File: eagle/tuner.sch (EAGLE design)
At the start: 32 parts, among them IC1 MEGA8-AI, IC2 LM358D, IC3 7805TV, M1 MIC

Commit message: updated PCB
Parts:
- removed M1: MIC, microphon:ELECTRET_MICROPHON-WM.64PN
- removed S1: POWER, switch:TL32YO
- removed S2: (no value), switch-omron:10-XX
- removed SG1: BUZZER, buzzer:F/QMB
- removed TP1, TP2: PTR1B1,27, testpad:PTR1B1,27
- added C10, C14, C15, C22, C23: 0.1uF, eagle-ltspice:C
- added C11, C12, C13: 1uF, eagle-ltspice:C
- added C16, C17, C18, C19: 47uF, rcl:CPOL-EUE2.5-5
- added C20: 470uF, rcl:CPOL-EUE3.5-8
- added C9: 470pF, eagle-ltspice:C
- added IN, OUT: (no value), pinhead:PINHD-1X2
- added R12, R13, R16, R17, R18, R19: 10k, resistor:R-EU_M0805
- added R14, R15: 1k, resistor:R-EU_M0805
- added SEL, VOL: (no value), pinhead:PINHD-1X3
- added U1: LP2985AIM5-5.0, LP2985AIM5-5.0:LP2985AIM5-5.0
- C2: value 0.1uF -> 2.2uF
- IC2: value LM358D -> LM358N; device linear:LM358D -> linear:LM358N
- IC3: value 7805TV -> AD811N; device linear:7805TV -> analog-devices:AD811N
- R10, R4: value 220k -> 10k
- R11: value 220k -> 20k
- R2: value 2.2k -> 100k
- R3: value (none) -> 100k; device resistor:R-TRIMM4G/J -> resistor:R-EU_M0805
- R5, R8: value 2.2k -> 10k
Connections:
- removed net RX: IC1.PD0(RXD), TP1.TP
- removed net TX: IC1.PD1(TXD), TP2.TP
- removed net V/2: IC2A.+IN, IC2B.+IN, R6.2, R7.1
- removed net VCC: C2.1, C3.2, IC1.VCC@1, IC1.VCC@2, IC2P.V+, IC3.VO, L1.1, R1.1, R10.2, R7.2, R8.2, S2.S, S2.S1, SV1.5
- new net 2.5V: C18.-, C19.+, IC2B.+IN, R4.1, R6.2, R7.1
- new net 4.5V: C16.-, C17.+, IC3.IN+, R12.2, R13.1
- new net 5V: C18.+, C2.1, C3.2, C8.2, IC1.VCC@1, IC1.VCC@2, L1.1, R1.1, R18.2, R19.2, R7.2, SV1.5, U1.VOUT
- new net 9V: C1.1, C16.+, G1.+, IC2P.V+, IC3.+VS, R13.2, R3.2, U1.ON/OFF, U1.VIN
- new net CLICK: C10.1, IC1.PD2(INT0)
- new net COUNT: C23.2, IC1.PD7(AIN1), R17.2, R19.1
- new net INSTR: C12.1, IC2A.OUT, R14.2, R4.2, R5.1
- new net N$11: IC3.IN-, R10.2, R11.2, R8.1, R9.2
- new net N$19: C15.1, R15.2, VOL.1
- new net N$20: IC2B.-IN, VOL.2
- new net N$21: C20.-, OUT.2
- new net N$23: R16.1, SEL.1
- new net N$24: R17.1, SEL.3
- new net PHASE: C22.1, IC1.PD6(AIN0), R16.2, R18.1
- new net TUNE: C11.1, IC2B.OUT, VOL.3
- net GND: now also C14.1, C15.2, C17.-, C19.-, C22.2, C23.1, C8.1, C9.2, IC3.-VS, IN.1, OUT.1, R12.1, R2.1, SEL.2, U1.GND; no longer IC3.GND, M1.2, R11.1, R9.1, SG1.-
- net N$10: now also C13.1, IC2A.+IN, R2.2, R3.1; no longer IC1.PC0(ADC0), IC2A.OUT, R3.A
- net N$12: now also C13.2, IN.2; no longer IC2B.OUT, R2.2, R4.1
- net N$13: now also IC2A.-IN, R5.2; no longer IC2B.-IN, R4.2, R5.1
- net N$14: now also C10.2, R9.1; no longer C8.2, M1.1, R8.1
- net N$15: now also C14.2, IC1.PC0(ADC0), R14.1; no longer C8.1, R10.1, R11.2, R5.2
- net N$16: now also C11.2, R10.1; no longer G1.+, S1.P
- net N$17: now also C12.2, R11.1; no longer IC1.PD3(INT1), R9.2, S2.P, S2.P1
- net N$18: now also IC1.PD3(INT1), R15.1; no longer IC2A.-IN, R2.1, R3.S
- net N$2: now also C9.1, U1.BY_PASS; no longer C1.1, IC3.VI, S1.O
- net N$9: now also C20.+, IC3.OUT, R8.2; no longer IC1.PD2(INT0), SG1.+
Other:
- moved on the sheet: C1, C2, C3, C8, G1, IC2A, IC2B, R10, R11, R2, R4, R5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

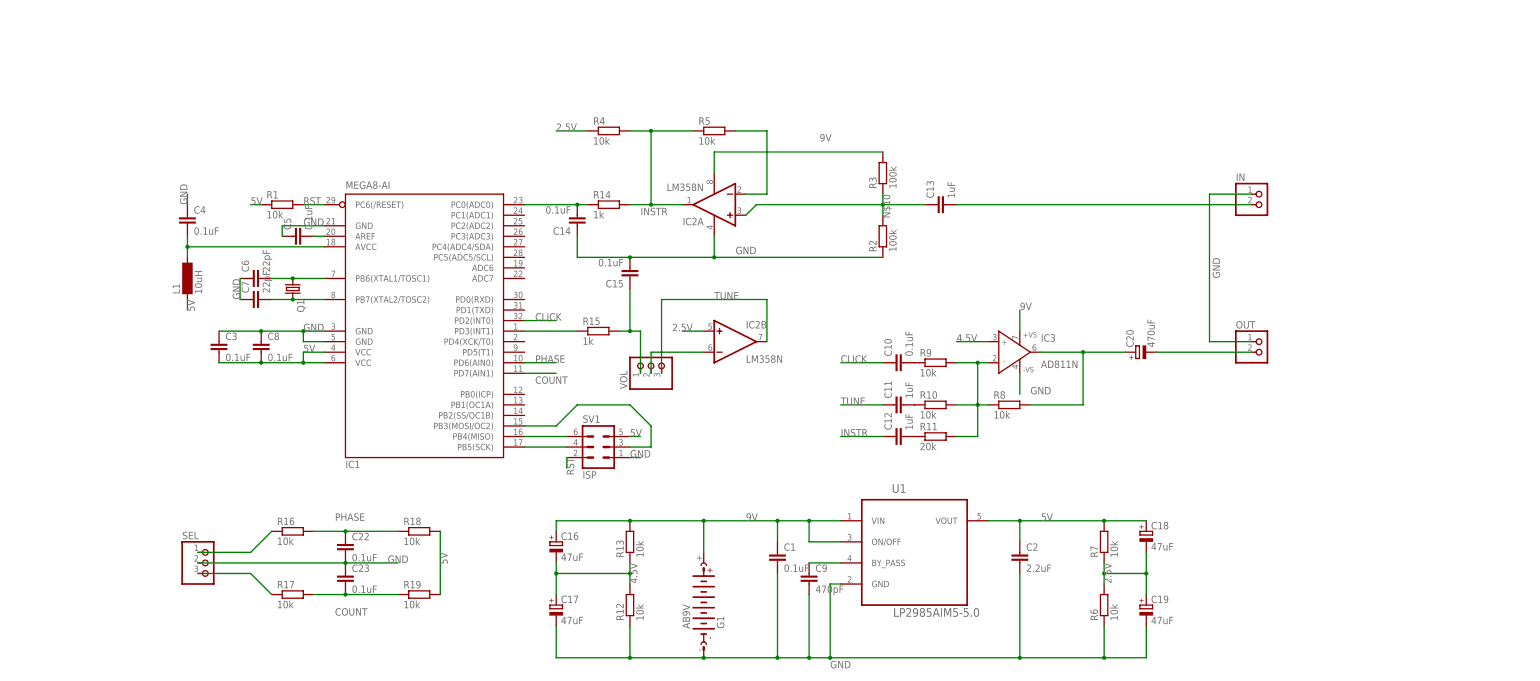
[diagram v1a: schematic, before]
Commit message: update schematic with agc and high-z input, D-class out
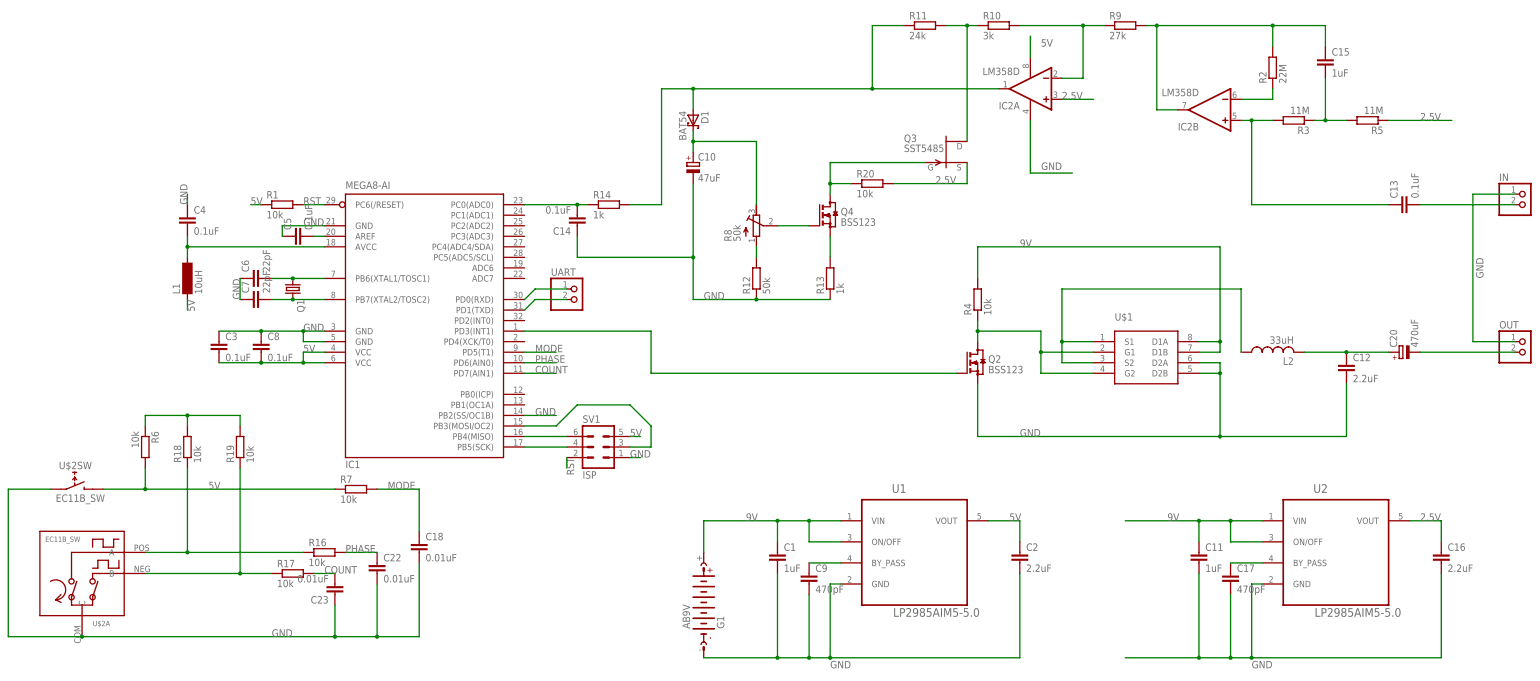
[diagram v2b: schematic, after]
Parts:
- removed C19: 47uF, rcl:CPOL-EUE2.5-5
- removed IC3: AD811N, analog-devices:AD811N
- removed R15: 1k, resistor:R-EU_M0805
- removed SEL, VOL: (no value), pinhead:PINHD-1X3
- added D1: BAT54, diode:BAT54
- added L2: 33uH, rcl:L-US6000-XXX-RC
- added Q2, Q4: BSS123, transistor-small-signal:BSS123
- added Q3: SST5485, transistor-fet:SST5485
- added R20: 10k, resistor:R-EU_M0805
- added U$1: IRF9389TRPBF, IRF9389TRPBF:IRF9389TRPBF
- added U$2: EC11B_SW, rotary-encoder:EC11B_SW
- added U2: LP2985AIM5-5.0, LP2985AIM5-5.0:LP2985AIM5-5.0
- added UART: (no value), pinhead:PINHD-1X2
- C1, C15: value 0.1uF -> 1uF
- C10: value 0.1uF -> 47uF; device eagle-ltspice:C -> rcl:CPOL-EUE2-5
- C12: value 1uF -> 2.2uF
- C13: value 1uF -> 0.1uF
- C16: value 47uF -> 2.2uF; device rcl:CPOL-EUE2.5-5 -> eagle-ltspice:C
- C17: value 47uF -> 470pF; device rcl:CPOL-EUE2.5-5 -> eagle-ltspice:C
- C18: value 47uF -> 0.01uF; device rcl:CPOL-EUE2.5-5 -> eagle-ltspice:C
- C22, C23: value 0.1uF -> 0.01uF
- IC2: value LM358N -> LM358D; device linear:LM358N -> linear:LM358D
- R10: value 10k -> 3k
- R11: value 20k -> 24k
- R12: value 10k -> 50k
- R13: value 10k -> 1k
- R2: value 100k -> 22M
- R3: value 100k -> 11M
- R5: value 10k -> 11M
- R8: value 10k -> 50k; device resistor:R-EU_M0805 -> rcl:R-TRIMM4G/J
- R9: value 10k -> 27k
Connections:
- removed net 4.5V: C16.-, C17.+, IC3.IN+, R12.2, R13.1
- removed net CLICK: C10.1, IC1.PD2(INT0)
- removed net INSTR: C12.1, IC2A.OUT, R14.2, R4.2, R5.1
- removed net TUNE: C11.1, IC2B.OUT, VOL.3
- new net MODE: C18.1, IC1.PD5(T1), R7.2
- new net N$26: IC1.PD0(RXD), UART.1
- new net N$27: D1.A, IC2A.OUT, R11.1, R14.2
- new net N$28: IC1.PD1(TXD), UART.2
- new net N$29: C10.+, D1.C, R8.E
- new net N$30: R12.2, R8.A
- new net N$31: Q4.G, R8.S
- new net N$32: Q4.S, R13.2
- new net N$33: Q3.G, Q4.D, R20.1
- new net N$34: C17.1, U2.BY_PASS
- new net N$35: R6.2, R7.1, U$2SW.E
- net 2.5V: now also C16.1, IC2A.+IN, Q3.S, R20.2, R5.1, U2.VOUT; no longer C18.-, C19.+, IC2B.+IN, R4.1, R6.2, R7.1
- net 5V: now also IC2P.V+, R6.1; no longer C18.+, R7.2
- net 9V: now also C11.1, R4.2, U$1.D1A, U$1.D1B, U2.ON/OFF, U2.VIN; no longer C16.+, IC2P.V+, IC3.+VS, R13.2, R3.2
- net COUNT: no longer R19.1
- net GND: now also C10.-, C11.2, C12.2, C16.2, C17.2, C18.2, IC1.PB2(SS/OC1B), Q2.S, R13.1, U$1.D2A, U$1.D2B, U$2A.C, U$2SW.D, U2.GND; no longer C15.2, C17.-, C19.-, IC3.-VS, R2.1, R6.1, SEL.2
- net N$10: now also C15.1, IC2B.OUT, R9.2; no longer C13.1, IC2A.+IN, R3.1
- net N$11: now also L2.1, U$1.S1, U$1.S2; no longer IC3.IN-, R10.2, R11.2, R8.1, R9.2
- net N$13: now also IC2B.-IN, R2.1; no longer IC2A.-IN, R5.2
- net N$14: now also C12.1, C20.+, L2.2; no longer C10.2, R9.1
- net N$16: now also C13.1, IC2B.+IN, R3.2; no longer C11.2, R10.1
- net N$17: now also C15.2, R3.1, R5.2; no longer C12.2, R11.1
- net N$18: now also Q2.G; no longer R15.1
- net N$19: now also IC2A.-IN, R10.2, R9.1; no longer C15.1, R15.2, VOL.1
- net N$20: now also Q3.D, R10.1, R11.2; no longer IC2B.-IN, VOL.2
- net N$23: now also R18.1, U$2A.A; no longer SEL.1
- net N$24: now also R19.1, U$2A.B; no longer SEL.3
- net N$9: now also Q2.D, R4.1, U$1.G1, U$1.G2; no longer C20.+, IC3.OUT, R8.2
- net PHASE: no longer R18.1
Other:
- moved on the sheet: C11, C12, C13, C15, C20, C22, C23, IC2A, IC2B, IN, OUT, R10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

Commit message: second revision
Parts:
- removed G1: AB9V, battery:AB9V
- added 9V: (no value), pinhead:PINHD-1X2
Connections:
- net 9V: now also 9V.1; no longer G1.+
- net GND: now also 9V.2; no longer G1.-
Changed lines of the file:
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@@
 <parts>
 <part name="IC1" library="atmel" deviceset="MEGA8" device="-AI"/>
-<part name="G1" library="battery" deviceset="AB9V" device=""/>
 <part name="C1" library="eagle-ltspice" deviceset="C" device="" value="1uF"/>
 <part name="C2" library="eagle-ltspice" deviceset="C" device="" value="2.2uF"/>
@@
 <part name="C18" library="eagle-ltspice" deviceset="C" device="" value="0.01uF"/>
 <part name="R7" library="resistor" deviceset="R-EU_" device="M0805" value="10k"/>
+<part name="9V" library="pinhead" library_urn="urn:adsk.eagle:library:325" deviceset="PINHD-1X2" device=""/>
 </parts>
 <sheets>
@@
 <instances>
 <instance part="IC1" gate="G$1" x="27.94" y="58.42"/>
-<instance part="G1" gate="G$1" x="96.52" y="-12.7" rot="MR90"/>
 <instance part="C1" gate="G$1" x="114.3" y="0"/>
 <instance part="C2" gate="G$1" x="172.72" y="0"/>
@@
 <instance part="C18" gate="G$1" x="27.94" y="2.54"/>
 <instance part="R7" gate="G$1" x="12.7" y="15.24"/>
+<instance part="9V" gate="G$1" x="93.98" y="-12.7"/>
 </instances>
 <busses>
@@
 </segment>
 <segment>
-<pinref part="G1" gate="G$1" pin="-"/>
 <wire x1="121.92" y1="-25.4" x2="114.3" y2="-25.4" width="0.1524" layer="91"/>
 <wire x1="114.3" y1="-25.4" x2="96.52" y2="-25.4" width="0.1524" layer="91"/>
@@
 <pinref part="C2" gate="G$1" pin="2"/>
 <wire x1="172.72" y1="-5.08" x2="172.72" y2="-25.4" width="0.1524" layer="91"/>
+<pinref part="9V" gate="G$1" pin="2"/>
+<wire x1="96.52" y1="-25.4" x2="96.52" y2="-12.7" width="0.1524" layer="91"/>
+<wire x1="96.52" y1="-12.7" x2="91.44" y2="-12.7" width="0.1524" layer="91"/>
 </segment>
 <segment>
@@
 <junction x="121.92" y="7.62"/>
 <junction x="114.3" y="7.62"/>
-<pinref part="G1" gate="G$1" pin="+"/>
 <wire x1="96.52" y1="7.62" x2="114.3" y2="7.62" width="0.1524" layer="91"/>
-<wire x1="96.52" y1="0" x2="96.52" y2="7.62" width="0.1524" layer="91"/>
+<pinref part="9V" gate="G$1" pin="1"/>
+<wire x1="96.52" y1="7.62" x2="96.52" y2="-10.16" width="0.1524" layer="91"/>
+<wire x1="96.52" y1="-10.16" x2="91.44" y2="-10.16" width="0.1524" layer="91"/>
 </segment>
 <segment>
@@
 <wire x1="83.82" y1="43.18" x2="83.82" y2="53.34" width="0.1524" layer="91"/>
 <wire x1="83.82" y1="53.34" x2="53.34" y2="53.34" width="0.1524" layer="91"/>
-</segment>
-</net>
-<net name="N$12" class="0">
-<segment>
-<pinref part="C13" gate="G$1" pin="2"/>
-<pinref part="IN" gate="G$1" pin="2"/>
-<wire x1="269.24" y1="83.82" x2="292.1" y2="83.82" width="0.1524" layer="91"/>
 </segment>
 </net>
@@
 </segment>
 </net>
+<net name="N$12" class="0">
+<segment>
+<pinref part="C13" gate="G$1" pin="2"/>
+<pinref part="IN" gate="G$1" pin="2"/>
+<wire x1="269.24" y1="83.82" x2="292.1" y2="83.82" width="0.1524" layer="91"/>
+</segment>
+</net>

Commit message: work on next revision PCB
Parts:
- removed D1: BAT54, diode:BAT54
- removed L1: 10uH, inductor-neosid:SM-1206
- removed L2: 33uH, rcl:L-US6000-XXX-RC
- removed Q2, Q4: BSS123, transistor-small-signal:BSS123
- removed Q3: SST5485, transistor-fet:SST5485
- removed U$1: IRF9389TRPBF, IRF9389TRPBF:IRF9389TRPBF
- added C19, C26: 1u, eagle-ltspice:C
- added C21, C24, C27: 0.1uF, eagle-ltspice:C
- added C25: 1uF, eagle-ltspice:C
- added D2: BAS40-04, diode:BAS40-04
- added IC3: LM358D, linear:LM358D
- added PASS, VOL: (no value), pinhead:PINHD-1X2
- added R15, R23: 1k, resistor:R-EU_M0805
- added R21, R22: 10k, resistor:R-EU_M0805
- added R24, R25: 100k, resistor:R-EU_M0805
- added TP1, TP2, TP3: PTR1B1,27, testpad:PTR1B1,27
- added U3: ADC121S021CIMF, ADC121S021CIMF:ADC121S021CIMF
- C10: value 47uF -> 96n; device rcl:CPOL-EUE2-5 -> eagle-ltspice:C
- C12: value 2.2uF -> 1uF
- C14: value 0.1uF -> 47n
- C15: value 1uF -> 47n
- C16: value 2.2uF -> 47n
- C17: value 470pF -> 47n
- C20: value 470uF -> 0.1uF; device rcl:CPOL-EUE3.5-8 -> eagle-ltspice:C
- R10: value 3k -> 68k
- R11: value 24k -> 34k
- R12: value 50k -> 0
- R13: value 1k -> 0
- R14: value 1k -> 259k
- R2: value 22M -> 10k
- R20: value 10k -> 1k
- R3: value 11M -> 10M
- R4: value 10k -> 259k
- R5: value 11M -> 10k
- R8: value 50k -> 68k; device rcl:R-TRIMM4G/J -> resistor:R-EU_M0805
- R9: value 27k -> 100k
- U2: value LP2985AIM5-5.0 -> SSM2305RMZ-R2; device LP2985AIM5-5.0:LP2985AIM5-5.0 -> SSM2305RMZ-R2:SSM2305RMZ-R2
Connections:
- net N$8 renamed MOSI
- removed net 2.5V: C16.1, IC2A.+IN, Q3.S, R20.2, R5.1, U2.VOUT
- removed net N$1: C4.2, IC1.AVCC, L1.2
- removed net N$33: Q3.G, Q4.D, R20.1
- removed net N$34: C17.1, U2.BY_PASS
- new net BUZZER: IC1.PD3(INT1), R25.1, VOL.2
- new net CS_ADC: IC1.PC1(ADC1), U3.~CS
- new net MISO: IC1.PB4(MISO), SV1.6, U3.SDATA
- new net N$8: C12.2, IC3A.+IN, IC3B.+IN, R21.2, R22.1
- new net SCK: IC1.PB5(SCK), SV1.4, U3.SCLK
- new net SD_AMP: IC1.PD2(INT0), U2.SD
- net 5V: now also C20.2, C21.2, C24.2, C27.2, C4.2, D2.C2, IC1.AVCC, IC3P.V+, R2.1, R21.1, U2.VDD, U3.VA; no longer L1.1
- net 9V: no longer C11.1, R4.2, U$1.D1A, U$1.D1B, U2.ON/OFF, U2.VIN
- net GND: now also C10.1, C11.1, C12.1, C20.1, C21.1, C24.1, C27.1, D2.A1, IC3P.V-, PASS.1, R11.1, R12.2, R22.2, R5.2, U2.NC, U3.GND; no longer C10.-, C11.2, C12.2, C14.1, C17.2, IC1.PB2(SS/OC1B), OUT.1, Q2.S, U$1.D2A, U$1.D2B
- net N$10: now also C14.1, R24.1, R8.2, R9.1, TP1.TP; no longer C15.1, R2.2, R9.2
- net N$11: now also OUT.2, U2.OUT-; no longer L2.1, U$1.S1, U$1.S2
- net N$13: now also R15.1, R9.2; no longer R2.1
- net N$14: now also R4.2, U2.IN+; no longer C12.1, C20.+, L2.2
- net N$15: now also C25.2, PASS.2; no longer C14.2, IC1.PC0(ADC0), R14.1
- net N$16: now also D2.C1A2
- net N$17: now also C11.2, R15.2, R2.2, R5.1; no longer C15.2, R5.2
- net N$18: now also C25.1, C26.1, IC3A.OUT, R20.2; no longer IC1.PD3(INT1), Q2.G
- net N$19: now also C14.2, C15.1, R11.2; no longer IC2A.-IN, R10.2, R9.1
- net N$20: now also C15.2, IC2A.+IN; no longer Q3.D, R11.2
- net N$21: now also R14.2, U2.IN-; no longer C20.-, OUT.2
- net N$27: now also C10.2, R10.2, R8.1; no longer D1.A, IC2A.OUT, R11.1, R14.2
- net N$29: now also C16.1, R14.1; no longer C10.+, D1.C, R8.E
- net N$30: now also IC2A.-IN, IC2A.OUT, R13.2, TP2.TP, U3.VIN; no longer R12.2, R8.A
- net N$31: now also C17.1, R4.1; no longer Q4.G, R8.S
- net N$32: now also C26.2, IC3A.-IN, R20.1, R24.2, R25.2; no longer Q4.S, R13.2
- net N$6: now also C17.2, C19.1, IC3B.OUT, R23.2, TP3.TP; no longer IC1.PB4(MISO), SV1.6
- net N$7: now also C19.2, IC3B.-IN, R23.1, VOL.1; no longer IC1.PB5(SCK), SV1.4
- net N$9: now also OUT.1, U2.OUT+; no longer Q2.D, R4.1, U$1.G1, U$1.G2
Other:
- moved on the sheet: 9V, C1, C11, C12, C13, C14, C15, C16, C17, C2, C3, C4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

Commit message: do board layout
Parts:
- added C28: 0.1u, eagle-ltspice:C
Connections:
- new net FG: C10.1, R11.1, R12.2, R13.1
- new net N$1: C28.1, R24.1
- net BUZZER: now also IC1.PB1(OC1A); no longer IC1.PD3(INT1)
- net GND: no longer C10.1, R11.1, R12.2, R13.1
- net N$10: now also C28.2; no longer R24.1
- net SD_AMP: now also IC1.PD3(INT1); no longer IC1.PD2(INT0)
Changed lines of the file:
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@@
 <part name="R25" library="resistor" deviceset="R-EU_" device="M0805" value="100k"/>
 <part name="C27" library="eagle-ltspice" deviceset="C" device="" value="0.1uF"/>
+<part name="C28" library="eagle-ltspice" deviceset="C" device="" value="0.1u"/>
 </parts>
 <sheets>
@@
 <instance part="R25" gate="G$1" x="195.58" y="30.48"/>
 <instance part="C27" gate="G$1" x="238.76" y="22.86"/>
+<instance part="C28" gate="G$1" x="185.42" y="73.66" rot="R180"/>
 </instances>
 <busses>
@@
 </segment>
 <segment>
-<pinref part="IC2" gate="P" pin="V-"/>
-<wire x1="99.06" y1="109.22" x2="99.06" y2="96.52" width="0.1524" layer="91"/>
-<wire x1="99.06" y1="96.52" x2="106.68" y2="96.52" width="0.1524" layer="91"/>
-<label x="106.68" y="99.06" size="1.778" layer="95" rot="R180"/>
-<pinref part="R12" gate="G$1" pin="1"/>
-<pinref part="R11" gate="G$1" pin="1"/>
-<pinref part="C10" gate="G$1" pin="1"/>
-<wire x1="106.68" y1="96.52" x2="114.3" y2="96.52" width="0.1524" layer="91"/>
-<wire x1="157.48" y1="106.68" x2="157.48" y2="111.76" width="0.1524" layer="91"/>
-<wire x1="157.48" y1="106.68" x2="114.3" y2="106.68" width="0.1524" layer="91"/>
-<junction x="157.48" y="106.68"/>
-<pinref part="R12" gate="G$1" pin="2"/>
-<wire x1="114.3" y1="106.68" x2="106.68" y2="106.68" width="0.1524" layer="91"/>
-<junction x="114.3" y="106.68"/>
-<wire x1="106.68" y1="106.68" x2="106.68" y2="96.52" width="0.1524" layer="91"/>
-<junction x="106.68" y="96.52"/>
-<pinref part="R13" gate="G$1" pin="1"/>
-<wire x1="114.3" y1="109.22" x2="114.3" y2="106.68" width="0.1524" layer="91"/>
-</segment>
-<segment>
 <label x="261.62" y="86.36" size="1.778" layer="95"/>
 <pinref part="C11" gate="G$1" pin="1"/>
@@
 <wire x1="238.76" y1="25.4" x2="238.76" y2="27.94" width="0.1524" layer="91"/>
 <label x="238.76" y="25.4" size="1.778" layer="95" rot="R90"/>
+</segment>
+<segment>
+<pinref part="R12" gate="G$1" pin="1"/>
+<pinref part="IC2" gate="P" pin="V-"/>
+<wire x1="99.06" y1="109.22" x2="99.06" y2="96.52" width="0.1524" layer="91"/>
+<wire x1="99.06" y1="96.52" x2="114.3" y2="96.52" width="0.1524" layer="91"/>
+<label x="106.68" y="99.06" size="1.778" layer="95" rot="R180"/>
 </segment>
 </net>
@@
 <wire x1="190.5" y1="106.68" x2="190.5" y2="104.14" width="0.1524" layer="91"/>
 <junction x="190.5" y="106.68"/>
-<pinref part="R24" gate="G$1" pin="1"/>
-<wire x1="190.5" y1="48.26" x2="185.42" y2="48.26" width="0.1524" layer="91"/>
-<wire x1="185.42" y1="48.26" x2="185.42" y2="106.68" width="0.1524" layer="91"/>
+<pinref part="C28" gate="G$1" pin="2"/>
+<wire x1="185.42" y1="101.6" x2="185.42" y2="78.74" width="0.1524" layer="91"/>
+<wire x1="185.42" y1="101.6" x2="185.42" y2="106.68" width="0.1524" layer="91"/>
 <junction x="185.42" y="106.68"/>
 </segment>
@@
 </segment>
 <segment>
-<pinref part="IC1" gate="G$1" pin="PD2(INT0)"/>
-<wire x1="17.78" y1="88.9" x2="27.94" y2="88.9" width="0.1524" layer="91"/>
-<label x="20.32" y="88.9" size="1.778" layer="95"/>
+<pinref part="IC1" gate="G$1" pin="PD3(INT1)"/>
+<wire x1="17.78" y1="86.36" x2="27.94" y2="86.36" width="0.1524" layer="91"/>
+<label x="20.32" y="86.36" size="1.778" layer="95"/>
 </segment>
 </net>
@@
 <net name="BUZZER" class="0">
 <segment>
-<pinref part="IC1" gate="G$1" pin="PD3(INT1)"/>
-<wire x1="17.78" y1="86.36" x2="27.94" y2="86.36" width="0.1524" layer="91"/>
-<label x="20.32" y="86.36" size="1.778" layer="95"/>
-</segment>
-<segment>
 <wire x1="134.62" y1="-17.78" x2="116.84" y2="-17.78" width="0.1524" layer="91"/>
 <label x="116.84" y="-17.78" size="1.778" layer="95"/>
@@
 <wire x1="190.5" y1="30.48" x2="172.72" y2="30.48" width="0.1524" layer="91"/>
 <label x="175.26" y="30.48" size="1.778" layer="95"/>
+</segment>
+<segment>
+<pinref part="IC1" gate="G$1" pin="PB1(OC1A)"/>
+<wire x1="17.78" y1="68.58" x2="27.94" y2="68.58" width="0.1524" layer="91"/>
+<label x="20.32" y="68.58" size="1.778" layer="95"/>
 </segment>
 </net>
@@
 </segment>
 </net>
+<net name="FG" class="0">
+<segment>
+<pinref part="R11" gate="G$1" pin="1"/>
+<pinref part="C10" gate="G$1" pin="1"/>
+<wire x1="157.48" y1="106.68" x2="157.48" y2="111.76" width="0.1524" layer="91"/>
+<wire x1="157.48" y1="106.68" x2="114.3" y2="106.68" width="0.1524" layer="91"/>
+<junction x="157.48" y="106.68"/>
+<pinref part="R12" gate="G$1" pin="2"/>
+<junction x="114.3" y="106.68"/>
+<pinref part="R13" gate="G$1" pin="1"/>
+<wire x1="114.3" y1="109.22" x2="114.3" y2="106.68" width="0.1524" layer="91"/>
+</segment>
+</net>
+<net name="N$1" class="0">
+<segment>
+<pinref part="R24" gate="G$1" pin="1"/>
+<wire x1="190.5" y1="48.26" x2="185.42" y2="48.26" width="0.1524" layer="91"/>
+<pinref part="C28" gate="G$1" pin="1"/>
+<wire x1="185.42" y1="71.12" x2="185.42" y2="48.26" width="0.1524" layer="91"/>
+</segment>
+</net>
